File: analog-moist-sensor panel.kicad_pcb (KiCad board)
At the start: 2 copper layers, 40.5 x 115.8 mm, 50 parts, among them P1 CONN_01X06, Q1 MOSFET_P, U1 NC7WZU04P6, U2 LM324, X1 16MHz

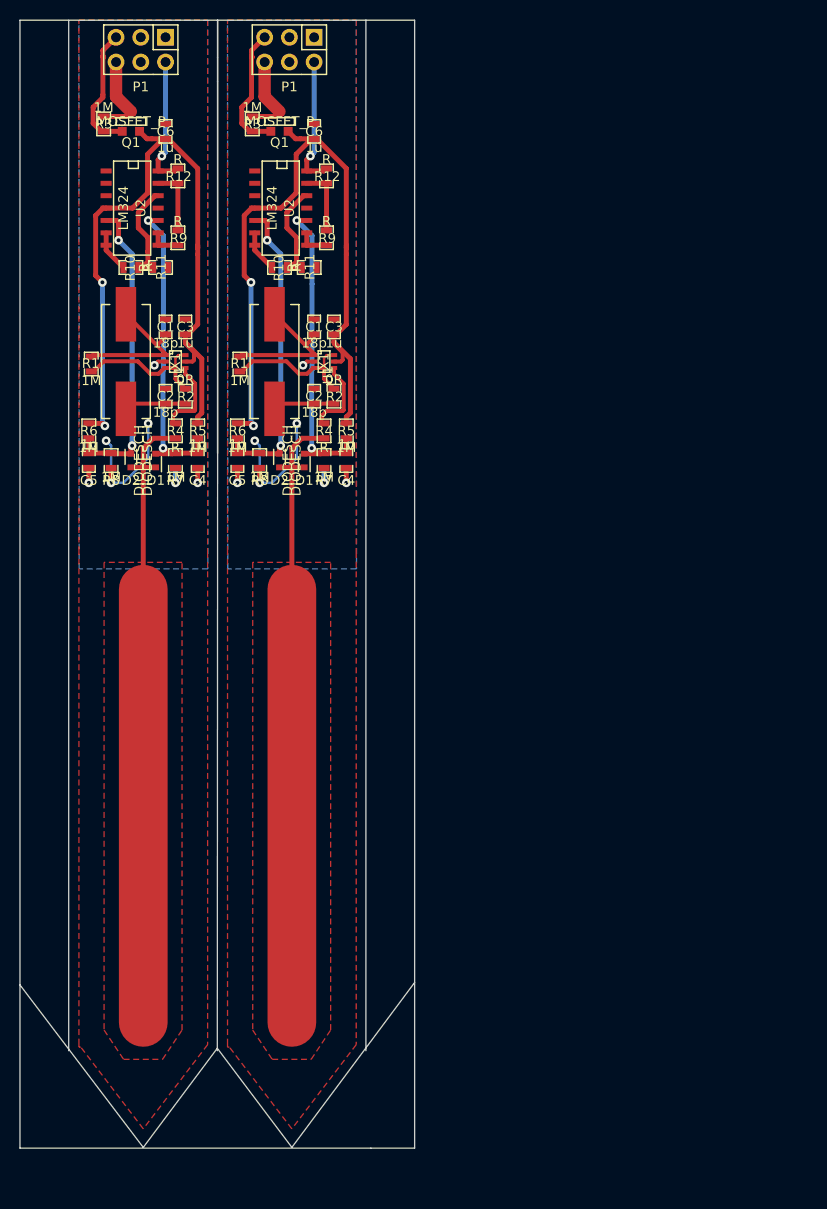
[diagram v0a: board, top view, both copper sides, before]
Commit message: Some forgotten changes before manufacturing
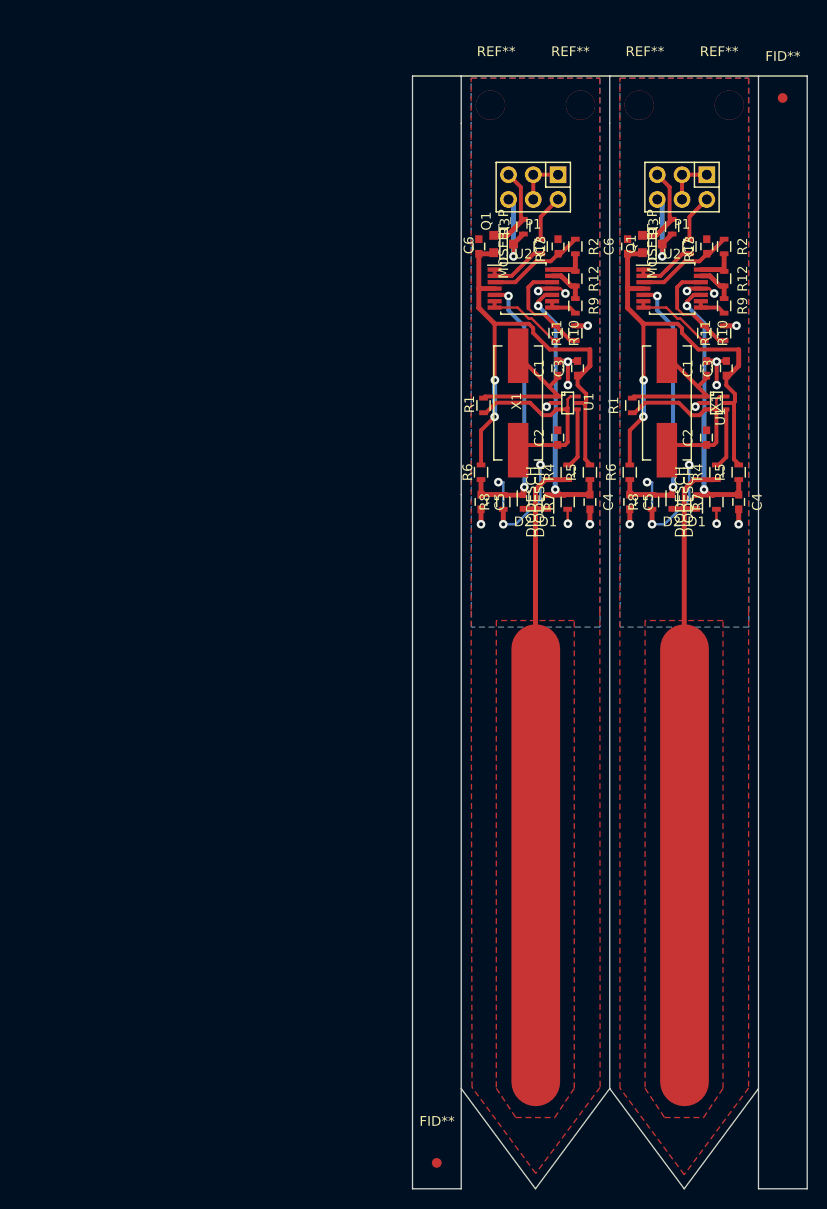
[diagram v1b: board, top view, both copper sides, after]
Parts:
- removed the C1 at (68.7, 54.0)
- removed the C1 at (83.9, 54.0)
- removed the C2 at (68.7, 61.1)
- removed the C2 at (83.9, 61.1)
- removed the C3 at (70.7, 54.0)
- removed the C3 at (86.0, 54.0)
- removed the C4 at (72.0, 67.7)
- removed the C4 at (87.2, 67.7)
- removed the C5 at (60.8, 67.7)
- removed the C5 at (76.1, 67.7)
- removed the C6 at (68.7, 33.9)
- removed the C6 at (83.9, 33.9)
- removed the D1 at (67.7, 67.7)
- removed the D1 at (82.9, 67.7)
- removed the D2 at (65.1, 67.7)
- removed the D2 at (80.4, 67.7)
- removed the P1 at (66.1, 25.5)
- removed the P1 at (81.4, 25.5)
- removed the Q1 at (65.1, 32.9)
- removed the Q1 at (80.4, 32.9)
- removed the R1 at (61.1, 57.8)
- removed the R1 at (76.3, 57.8)
- removed the R10 at (65.1, 47.9)
- removed the R10 at (80.4, 47.9)
- removed the R11 at (68.2, 47.9)
- removed the R11 at (83.4, 47.9)
- removed the R12 at (70.0, 38.5)
- removed the R12 at (85.2, 38.5)
- removed the R2 at (70.7, 61.1)
- removed the R2 at (86.0, 61.1)
- removed the R3 at (62.3, 33.1)
- removed the R3 at (77.6, 33.1)
- removed the R4 at (69.7, 64.6)
- removed the R4 at (85.0, 64.6)
- removed the R5 at (72.0, 64.6)
- removed the R5 at (87.2, 64.6)
- removed the R6 at (60.8, 64.6)
- removed the R6 at (76.1, 64.6)
- removed the R7 at (69.7, 67.7)
- removed the R7 at (85.0, 67.7)
- removed the R8 at (63.1, 67.7)
- removed the R8 at (78.3, 67.7)
- removed the R9 at (70.0, 44.8)
- removed the R9 at (85.2, 44.8)
- removed the U1 at (69.7, 57.5)
- removed the U1 at (85.0, 57.5)
- removed the U2 at (65.4, 41.8)
- removed the U2 at (80.6, 41.8)
- removed the X1 at (64.6, 57.5)
- removed the X1 at (79.9, 57.5)
- added C1: 18p, Capacitors_SMD:C_0603, F.Cu at (124.2, 58.2)
- added C1: 18p, Capacitors_SMD:C_0603, F.Cu at (108.9, 58.2)
- added C2: 18p, Capacitors_SMD:C_0603, F.Cu at (124.2, 65.3)
- added C2: 18p, Capacitors_SMD:C_0603, F.Cu at (108.9, 65.3)
- added C3: 1u, Capacitors_SMD:C_0603, F.Cu at (126.2, 58.2)
- added C3: 1u, Capacitors_SMD:C_0603, F.Cu at (111.0, 58.2)
- added C4: 1n, Capacitors_SMD:C_0603, F.Cu at (127.5, 71.9)
- added C4: 1n, Capacitors_SMD:C_0603, F.Cu at (112.2, 71.9)
- added C5: 1n, Capacitors_SMD:C_0603, F.Cu at (116.3, 71.9)
- added C5: 1n, Capacitors_SMD:C_0603, F.Cu at (101.1, 71.9)
- added C6: 1u, Capacitors_SMD:C_0603, F.Cu at (116.1, 45.7)
- added C6: 1u, Capacitors_SMD:C_0603, F.Cu at (100.8, 45.7)
- added C7: 1u, Capacitors_SMD:C_0603, F.Cu at (124.2, 45.7)
- added C7: 1u, Capacitors_SMD:C_0603, F.Cu at (109.0, 45.7)
- added D1: DIODESCH, SMD_Packages:SOD-523, F.Cu at (123.2, 71.9)
- added D1: DIODESCH, SMD_Packages:SOD-523, F.Cu at (107.9, 71.9)
- added D2: DIODESCH, SMD_Packages:SOD-523, F.Cu at (120.6, 71.9)
- added D2: DIODESCH, SMD_Packages:SOD-523, F.Cu at (105.4, 71.9)
- added FID**: Fiducial_Modern_CopperTop, Fiducials:Fiducial_Modern_CopperTop, F.Cu at (132.0, 30.5)
- added FID**: Fiducial_Modern_CopperTop, Fiducials:Fiducial_Modern_CopperTop, F.Cu at (96.5, 139.8)
- added P1: CONN_01X06, Pin_Headers:Pin_Header_Straight_2x03, F.Cu at (121.7, 39.6)
- added P1: CONN_01X06, Pin_Headers:Pin_Header_Straight_2x03, F.Cu at (106.4, 39.6)
- added Q1: MOSFET_P, SMD_Packages:SOT-23-GDS, F.Cu at (118.6, 45.5)
- added Q1: MOSFET_P, SMD_Packages:SOT-23-GDS, F.Cu at (103.4, 45.5)
- added R1: 1M, Resistors_SMD:R_0603, F.Cu at (116.6, 62.0)
- added R1: 1M, Resistors_SMD:R_0603, F.Cu at (101.3, 62.0)
- added R10: 10k 0.1%, Resistors_SMD:R_0603, F.Cu at (124.0, 54.6)
- added R10: 10k 0.1%, Resistors_SMD:R_0603, F.Cu at (108.7, 54.6)
- added R11: 10k 0.1%, Resistors_SMD:R_0603, F.Cu at (126.0, 54.6)
- added R11: 10k 0.1%, Resistors_SMD:R_0603, F.Cu at (110.7, 54.6)
- added R12: 10k 0.1%, Resistors_SMD:R_0603, F.Cu at (126.0, 49.0)
- added R12: 10k 0.1%, Resistors_SMD:R_0603, F.Cu at (110.7, 49.0)
- added R13: 330, Resistors_SMD:R_0603, F.Cu at (122.5, 45.7)
- added R13: 330, Resistors_SMD:R_0603, F.Cu at (107.2, 45.7)
- added R2: 10k, Resistors_SMD:R_0603, F.Cu at (126.0, 45.7)
- added R2: 10k, Resistors_SMD:R_0603, F.Cu at (110.7, 45.7)
- added R3: 1M, Resistors_SMD:R_0603, F.Cu at (120.7, 43.7)
- added R3: 1M, Resistors_SMD:R_0603, F.Cu at (105.4, 43.7)
- added R4: 330, Resistors_SMD:R_0603, F.Cu at (125.2, 68.9)
- added R4: 330, Resistors_SMD:R_0603, F.Cu at (110.0, 68.9)
- added R5: 1M, Resistors_SMD:R_0603, F.Cu at (127.5, 68.9)
- added R5: 1M, Resistors_SMD:R_0603, F.Cu at (112.2, 68.9)
- added R6: 1M, Resistors_SMD:R_0603, F.Cu at (116.3, 68.9)
- added R6: 1M, Resistors_SMD:R_0603, F.Cu at (101.1, 68.9)
- added R7: 1M, Resistors_SMD:R_0603, F.Cu at (125.2, 71.9)
- added R7: 1M, Resistors_SMD:R_0603, F.Cu at (110.0, 71.9)
- added R8: 1M, Resistors_SMD:R_0603, F.Cu at (118.6, 71.9)
- added R8: 1M, Resistors_SMD:R_0603, F.Cu at (103.3, 71.9)
- added R9: 10k 0.1%, Resistors_SMD:R_0603, F.Cu at (126.0, 51.8)
- added R9: 10k 0.1%, Resistors_SMD:R_0603, F.Cu at (110.7, 51.8)
- added REF**: MountingHole_3mm, Mounting_Holes:MountingHole_3mm, F.Cu at (125.5, 29.7)
- added REF**: MountingHole_3mm, Mounting_Holes:MountingHole_3mm, F.Cu at (117.9, 29.7)
- added REF**: MountingHole_3mm, Mounting_Holes:MountingHole_3mm, F.Cu at (102.6, 29.7)
- added REF**: MountingHole_3mm, Mounting_Holes:MountingHole_3mm, F.Cu at (110.2, 29.7)
- added U1: NC7WZU04P6, Transistors_SMD:sc70-6, F.Cu at (125.2, 61.8)
- added U1: NC7WZU04P6, Transistors_SMD:sc70-6, F.Cu at (110.0, 61.8)
- added U2: LM324, Housings_SSOP:TSSOP-14_4.4x5mm_Pitch0.65mm, F.Cu at (120.7, 50.0)
- added U2: LM324, Housings_SSOP:TSSOP-14_4.4x5mm_Pitch0.65mm, F.Cu at (105.4, 50.0)
- added X1: 16MHz, Crystals:Crystal_HC49-SD_SMD, F.Cu at (120.1, 61.8)
- added X1: 16MHz, Crystals:Crystal_HC49-SD_SMD, F.Cu at (104.9, 61.8)
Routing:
- net VCC: track 152.8 -> 102.7 mm
- net GND: track 37.6 -> 69.6 mm, vias 12 -> 24
- net Net-(R1-Pad1): track 30.9 -> 0.00 mm
- net Net-(C2-Pad1): track 13.4 -> 44.2 mm
- net Net-(C7-Pad1): track 0.00 -> 20.3 mm
- net /OUT: track 27.3 -> 9.62 mm, vias 2 -> 0
- net Net-(R13-Pad2): track 0.00 -> 13.0 mm
- net Net-(R10-Pad2): track 8.58 -> 17.6 mm
- net Net-(R12-Pad1): track 0.00 -> 8.52 mm
- net /~ENABLE: track 26.5 -> 18.1 mm
- net /SENSE_LOW: track 63.8 -> 58.2 mm
- net Net-(R12-Pad2): track 13.7 -> 8.21 mm
- net /SENSE_HIGH: track 62.2 -> 57.0 mm
- net /SENSOR_TRACK: track 129.9 -> 133.6 mm
- net Net-(R4-Pad2): track 16.6 -> 13.0 mm
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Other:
- board size 40.5 x 115.8 mm -> 40.5 x 114.2 mm
- net class Default: clearance 0.2286 -> 0.09
- rule trace_clearance: 0.2286 -> 0.09
- board text removed: "Analog soil moisture sensor v3.0 Albertas Mickenas mic@wemakethings.net"
